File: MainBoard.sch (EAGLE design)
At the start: 24 parts, among them U1 SN74HC595N, U2 LM1085IT-5.0/NOPB

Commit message: added SPI and 3.3 level
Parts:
- added B10, B11: SPARKFUN_LOGIC_LEVEL_CONVERTER, SparkFun-Boards:SPARKFUN_LOGIC_LEVEL_CONVERTER
- added C4, C5: 0.1uF, SparkFun-Capacitors:0.1UF-KIT-EZ-50V-20%
- added C6: (no value), rcl:C-US025-050X050
- added R1, R2, R3, R4, R5, R6, R7, R8: 100k, SparkFun-Resistors:100KOHM-HORIZ_KIT-1/4W-5%
- U1: value SN74HC595N -> LM1085IT-3.3/NOPBT03BM; device SparkFun-IC-Logic:74HC595N -> LM1085it-3.3:LM1085IT-3.3/NOPBT03BM
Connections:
- removed net N$39: B7.EN(CFG6), U1.QB
- new net 3.3V: B10.LV, B11.LV, B9.LV, C5.1, C6.1, PCB1.3V3@1, R1.1, R2.1, R3.1, R4.1, R5.1, R6.1, R7.1, R8.1, U1.VOUT
- new net N$2: B1.CFG2/SCK, B2.CFG2/SCK, B3.CFG2/SCK, B4.CFG2/SCK, B5.CFG2/SCK, B6.CFG2/SCK, B7.CFG2/SCK, B8.CFG2/SCK, U$1.D13
- new net N$38: B10.LV_RXO_2, B7.EN(CFG6), R7.2
- new net N$55: B11.HV_RXI_2, U$1.A2
- new net N$56: B11.HV_TXO_2, U$1.A3
- new net N$57: B10.HV_TXO_1, U$1.A4
- new net N$58: B10.HV_RXI_1, U$1.A5
- new net N$59: B10.HV_RXI_2, U$1.A6
- new net N$60: B10.HV_TXO_2, U$1.A7
- net GND: now also B10.GND, B10.GND@2, B11.GND, B11.GND@2, C4.2, C5.2, C6.2, PCB1.GND@25, PCB1.GND@30, PCB1.GND@34, PCB1.GND@39, U1.ADJ/GND; no longer U1.G, U1.GND
- net N$3: now also B10.LV_TXI_1, R5.2; no longer U1.QD
- net N$4: now also B10.LV_RXO_1, R6.2; no longer U1.QC
- net N$40: now also B10.LV_TXI_2, R8.2; no longer U1.QA
- net N$41: now also B11.LV_TXI_2, R4.2; no longer U1.QE
- net N$42: now also B11.LV_RXO_2, R3.2; no longer U1.QF
- net N$43: now also B11.LV_RXO_1, R2.2; no longer U1.QG
- net N$44: now also B11.LV_TXI_1, R1.2; no longer U1.QH
- net N$45: now also B1.CFG0/SD0, B2.CFG0/SD0, B3.CFG0/SD0, B4.CFG0/SD0, B5.CFG0/SD0, B6.CFG0/SD0, B7.CFG0/SD0, B8.CFG0/SD0, U$1.D12; no longer B9.LV, PCB1.3V3@1
- net N$46: now also B1.CFG1/SDI, B2.CFG1/SDI, B3.CFG1/SDI, B4.CFG1/SDI, B5.CFG1/SDI, B6.CFG1/SDI, B7.CFG1/SDI, B8.CFG1/SDI, U$1.D11; no longer U$1.A2, U1.RCK
- net N$47: now also B11.HV_TXO_1, U$1.A0; no longer U$1.A3, U1.SCK
- net N$48: now also B11.HV_RXI_1, U$1.A1; no longer U$1.A4, U1.SER
- net N$49: now also U$1.D8; no longer U$1.A5
- net N$50: now also U$1.D9; no longer U$1.A6
- net VCC: now also B10.HV, B11.HV; no longer U1.SCL, U1.VCC
- net VCCIO: now also C4.1
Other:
- moved on the sheet: B9

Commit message: Added Pi Power Dictatorship
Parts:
- added C7, C8: 0.1uF, SparkFun-Capacitors:0.1UF-KIT-EZ-50V-20%
- added C9: (no value), rcl:C-US025-050X050
- added K2: G2REA, relay:G2REA
- added U3: LM1085IT-5.0/NOPB, LM1085:LM1085IT-5.0/NOPB
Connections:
- new net N$39: C8.1, C9.1, PCB1.5V@2, PCB1.5V@4, U3.VOUT
- new net N$61: B1.VM, B2.VM, B3.VM, B4.VM, B5.VM, B6.VM, B7.VM, B8.VM, C1.1, C4.1, K22.P, K22.P@1, U2.VIN
- new net N$62: K21.1, PCB1.GPIO21
- net GND: now also C7.2, C8.2, C9.2, K21.2, U3.ADJ/GND
- net VCC: no longer PCB1.5V@2, PCB1.5V@4
- net VCCIO: now also C7.1, K22.S, K22.S@1, U3.VIN; no longer B1.VM, B2.VM, B3.VM, B4.VM, B5.VM, B6.VM, B7.VM, B8.VM, C1.1, C4.1, U2.VIN

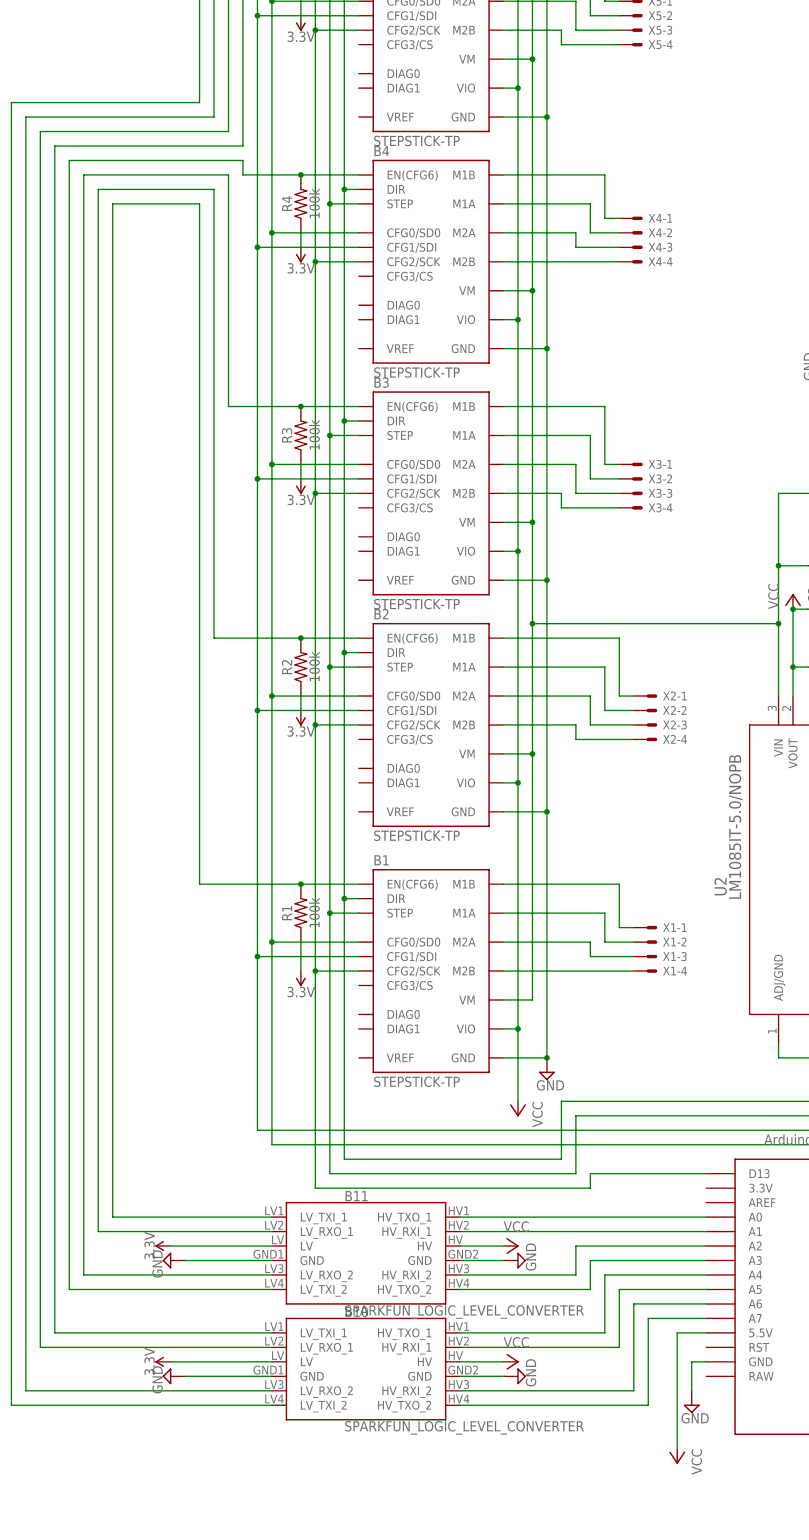
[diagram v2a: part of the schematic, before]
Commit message: Removed level-shifters
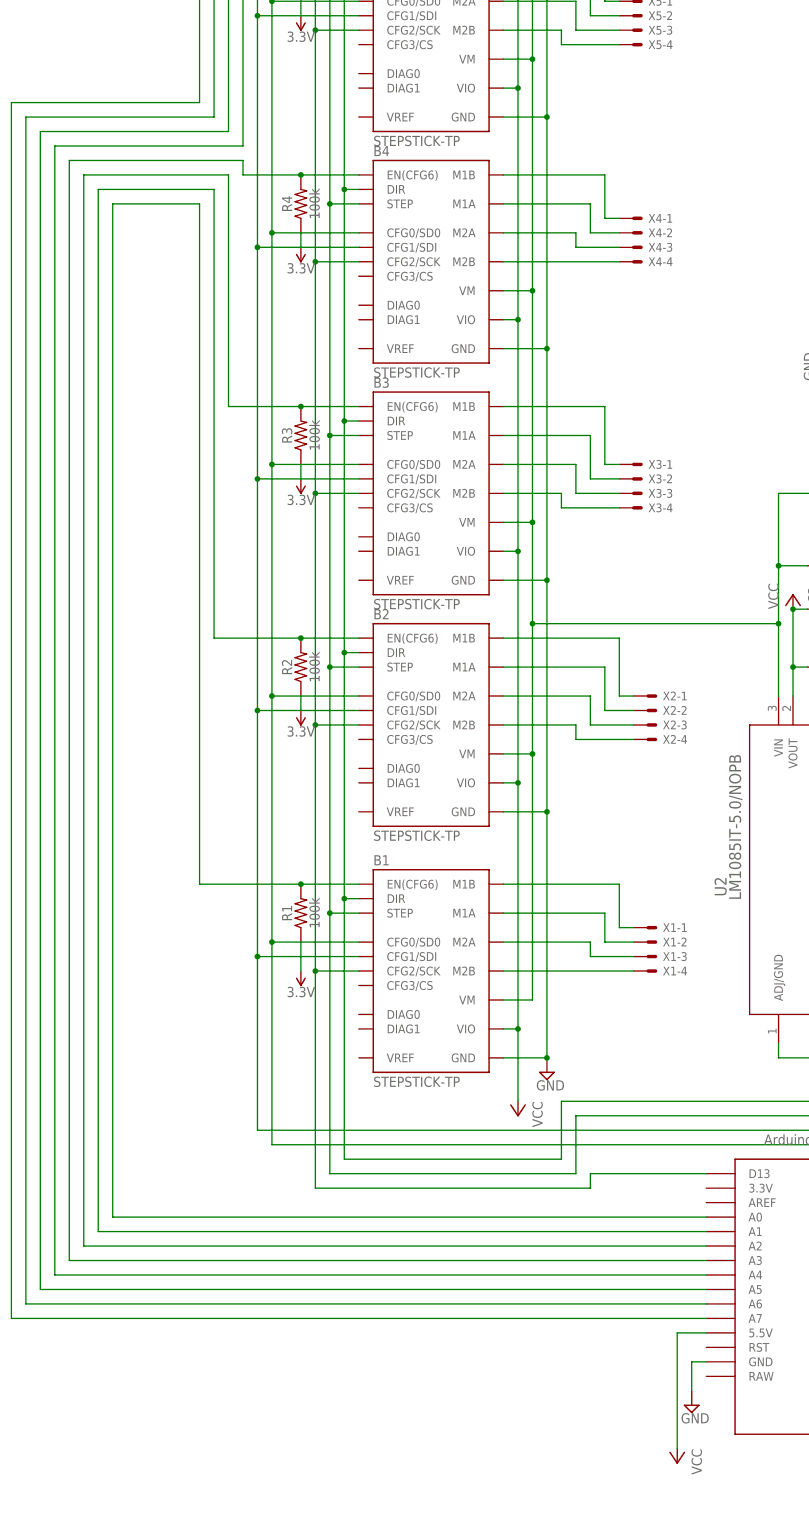
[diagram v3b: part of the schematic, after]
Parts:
- removed B10, B11: SPARKFUN_LOGIC_LEVEL_CONVERTER, SparkFun-Boards:SPARKFUN_LOGIC_LEVEL_CONVERTER
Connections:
- removed net N$47: B11.HV_TXO_1, U$1.A0
- removed net N$48: B11.HV_RXI_1, U$1.A1
- removed net N$55: B11.HV_RXI_2, U$1.A2
- removed net N$56: B11.HV_TXO_2, U$1.A3
- removed net N$57: B10.HV_TXO_1, U$1.A4
- removed net N$58: B10.HV_RXI_1, U$1.A5
- removed net N$59: B10.HV_RXI_2, U$1.A6
- removed net N$60: B10.HV_TXO_2, U$1.A7
- net 3.3V: no longer B10.LV, B11.LV
- net GND: no longer B10.GND, B10.GND@2, B11.GND, B11.GND@2
- net N$3: now also U$1.A4; no longer B10.LV_TXI_1
- net N$38: now also U$1.A6; no longer B10.LV_RXO_2
- net N$4: now also U$1.A5; no longer B10.LV_RXO_1
- net N$40: now also U$1.A7; no longer B10.LV_TXI_2
- net N$41: now also U$1.A3; no longer B11.LV_TXI_2
- net N$42: now also U$1.A2; no longer B11.LV_RXO_2
- net N$43: now also U$1.A1; no longer B11.LV_RXO_1
- net N$44: now also U$1.A0; no longer B11.LV_TXI_1
- net N$61: now also U1.VIN
- net VCC: no longer B10.HV, B11.HV
